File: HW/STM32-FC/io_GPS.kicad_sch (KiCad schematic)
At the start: 4 parts, among them J2 2.54mm Male, Q1 S9013

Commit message: 250102:STM32F407VET
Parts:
- removed J2: 2.54mm Male, Connector_PinHeader_2.54mm:PinHeader_1x03_P2.54mm_Vertical, symbol Connector_Generic:Conn_01x05
- removed Q1: S9013, digikey-footprints:SOT-23-3, symbol Device:Q_NPN_BEC
- removed R5: 1k, Resistor_SMD:R_0402_1005Metric, symbol Device:R_Small_US
- removed R6: 10k, Resistor_SMD:R_0402_1005Metric, symbol Device:R_Small_US
- added J12: Conn_01x06, Connectors_JST:JST_GH_BM06B-GHS-TBT_06x1.25mm_Straight, symbol Connector_Generic:Conn_01x06
- added J13: Conn_01x10, Connectors_JST:JST_GH_BM06B-GHS-TBT_06x1.25mm_Straight, symbol Connector_Generic:Conn_01x10
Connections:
- net +3.3V: now also J13.8 (Pin_8)
- net +5V: now also J12.1 (Pin_1), J13.1 (Pin_1)
- net GND: now also J12.6 (Pin_6), J13.10 (Pin_10)
- new net GPS1_BUZZER: J13.9 (Pin_9)
- new net GPS1_I2C_SCL: J13.4 (Pin_4)
- new net GPS1_I2C_SDA: J13.5 (Pin_5)
- new net GPS1_SW: J13.6 (Pin_6)
- new net GPS1_SW_LED: J13.7 (Pin_7)
- new net GPS1_UART_RX: J13.3 (Pin_3)
- new net GPS1_UART_TX: J13.2 (Pin_2)
- new net GPS2_I2C_SCL: J12.4 (Pin_4)
- new net GPS2_I2C_SDA: J12.5 (Pin_5)
- new net GPS2_UART_RX: J12.3 (Pin_3)
- new net GPS2_UART_TX: J12.2 (Pin_2)
- no-connect marks 1 -> 0

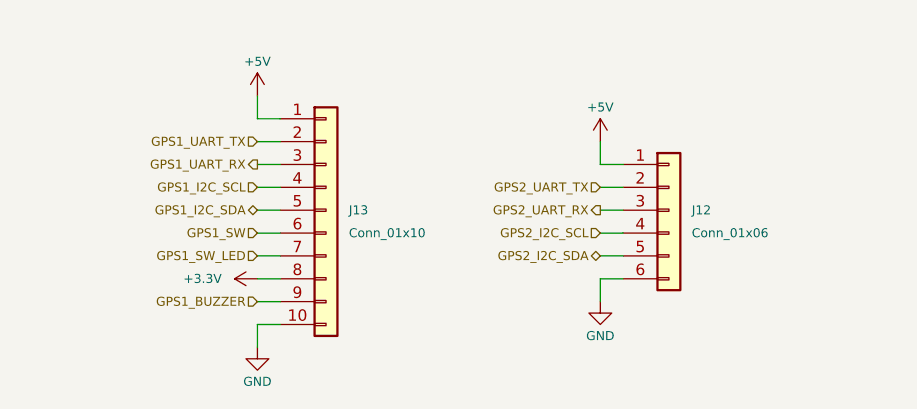
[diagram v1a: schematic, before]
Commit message: RC IN modified
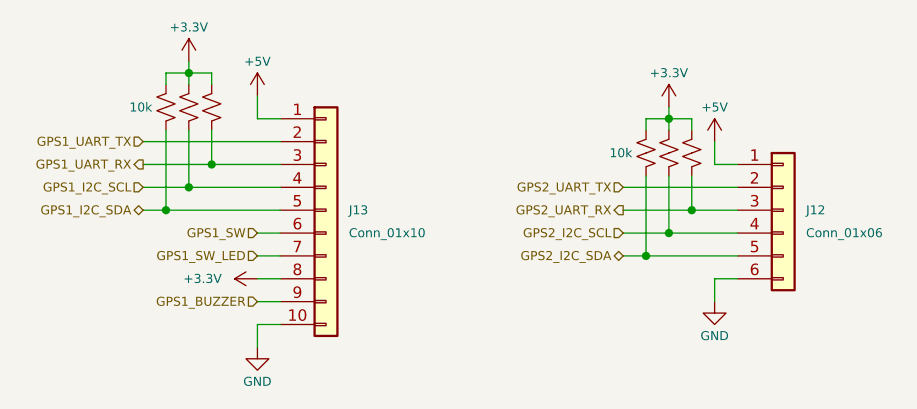
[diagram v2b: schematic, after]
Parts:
- added R18, R19, R20, R21, R22, R4: 10k, Resistor_SMD:R_0402_1005Metric, symbol Device:R_Small_US
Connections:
- net +3.3V: now also R18.1, R19.1, R20.1, R21.1, R22.1, R4.1
- net GPS1_I2C_SCL: now also R18.2
- net GPS1_I2C_SDA: now also R19.2
- net GPS1_UART_RX: now also R4.2
- net GPS2_I2C_SCL: now also R21.2
- net GPS2_I2C_SDA: now also R20.2
- net GPS2_UART_RX: now also R22.2
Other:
- moved on the sheet: J12

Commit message: Big Update:IMU/RC/Conn./MCU
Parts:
- J10: renamed from J12; value Conn_01x06 -> GPS2
- J9: renamed from J13; value Conn_01x10 -> GPS1; footprint Connectors_JST:JST_GH_BM06B-GHS-TBT_06x1.25mm_Straight -> Connectors_JST:JST_GH_BM10B-GHS-TBT_10x1.25mm_Straight
- renumbered R19 to R16, R18 to R17, R20 to R18, R4 to R19, R21 to R20, R22 to R21
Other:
- note added: "GH 1.25mm 10P PC10 : UART4_TX PC11 : UART4_RX PB8 : I2C1_SCL PB9 : I2C1_SDA"
- note added: "GH 1.25mm 6P PC12 : UART5_TX PD2 : UART5_RX PB10 : I2C2_SCL PB11 : I2C2_SDA"
- note added: "GPS1"
- note added: "GPS2"
- company: (none) -> INHA UNIV. NARAE
- title: (none) -> GPS
- moved on the sheet: J10, J9

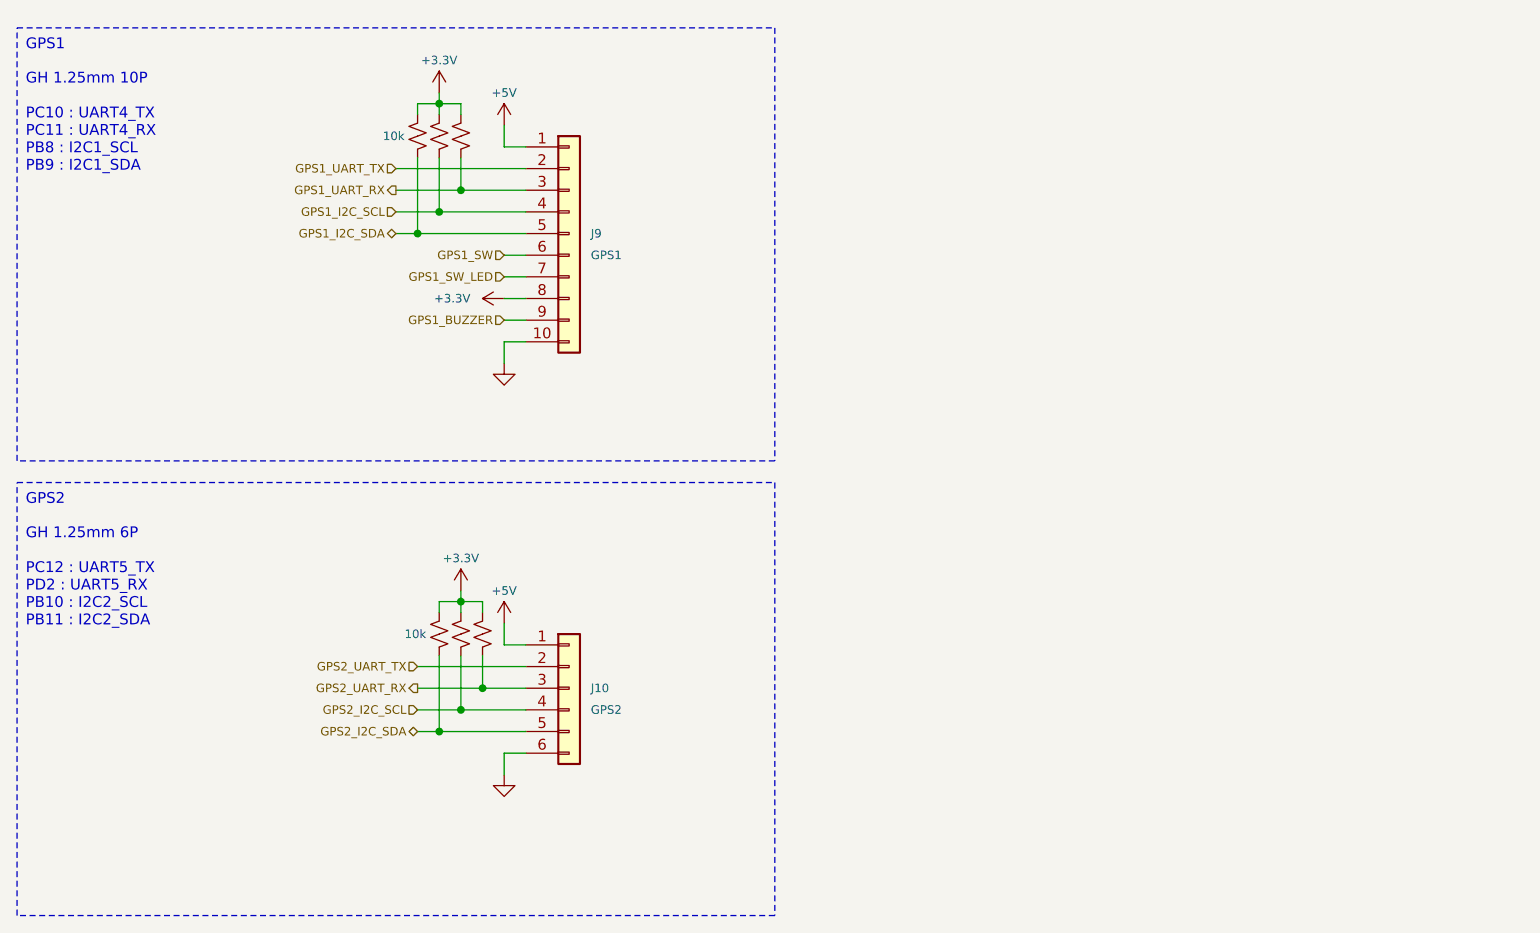
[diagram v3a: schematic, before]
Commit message: 2025.01.03v2:PM(Power Module) added
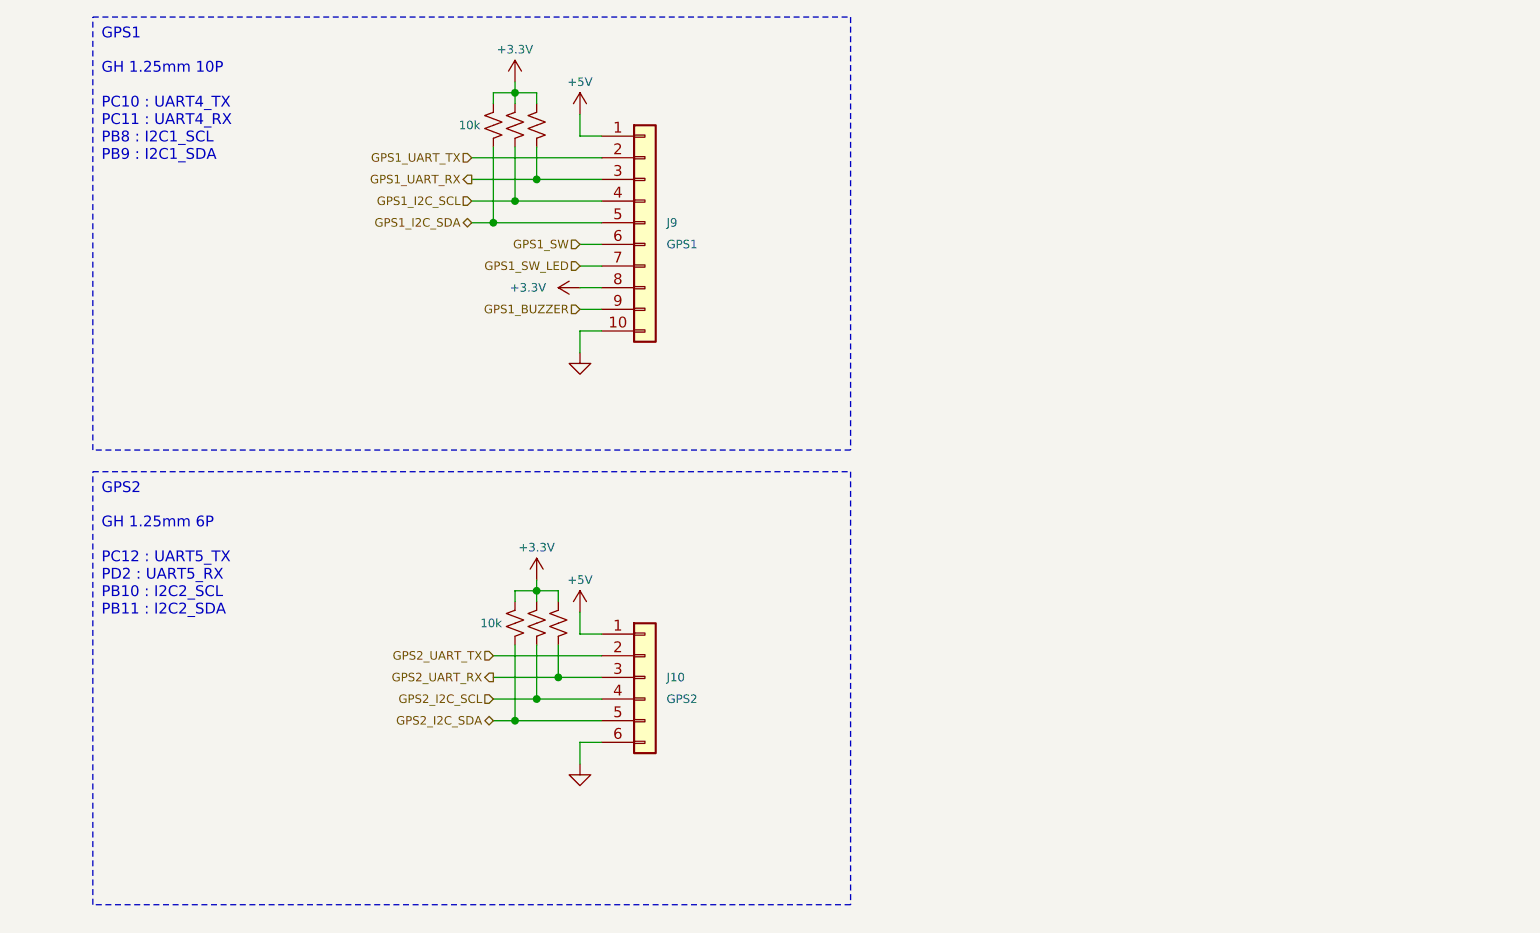
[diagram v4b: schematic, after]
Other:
- company: INHA UNIV. NARAE -> NARAE
- moved on the sheet: J10, J9

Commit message: Baro/SD Card update
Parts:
- J12: renamed from J9; value GPS1 -> GH 1.25mm 10P; footprint Connectors_JST:JST_GH_BM10B-GHS-TBT_10x1.25mm_Straight -> JST_GH:JST_GH_BM10B-GHS-TBT_10
- J13: renamed from J10; value GPS2 -> GH 1.25mm 6P; footprint Connectors_JST:JST_GH_BM06B-GHS-TBT_06x1.25mm_Straight -> JST_GH:JST_GH_BM06B-GHS-TBT_06
- renumbered R16 to R22, R17 to R23, R18 to R24, R19 to R25, R20 to R26, R21 to R27

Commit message: 2025.01.16
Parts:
- renumbered R25 to R24, R24 to R25

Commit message: 2025.01.17 : PCB layout
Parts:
- renumbered J13 to J10, J12 to J9, R22 to R23, R23 to R24, R24 to R26, R26 to R27, R27 to R28
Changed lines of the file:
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@@
 		(shape input)
 		(at 67.31 34.29 180)
-		(fields_autoplaced yes)
 		(effects
 			(font
@@
 		(shape bidirectional)
 		(at 69.85 95.25 180)
-		(fields_autoplaced yes)
 		(effects
 			(font
@@
 		(shape input)
 		(at 80.01 39.37 180)
-		(fields_autoplaced yes)
 		(effects
 			(font
@@
 		(shape input)
 		(at 80.01 41.91 180)
-		(fields_autoplaced yes)
 		(effects
 			(font
@@
 		(shape input)
 		(at 67.31 29.21 180)
-		(fields_autoplaced yes)
 		(effects
 			(font
@@
 		(shape output)
 		(at 67.31 31.75 180)
-		(fields_autoplaced yes)
 		(effects
 			(font
@@
 		(shape bidirectional)
 		(at 67.31 36.83 180)
-		(fields_autoplaced yes)
 		(effects
 			(font
@@
 		(shape input)
 		(at 69.85 92.71 180)
-		(fields_autoplaced yes)
 		(effects
 			(font
@@
 		(shape input)
 		(at 80.01 46.99 180)
-		(fields_autoplaced yes)
 		(effects
 			(font
@@
 		(shape input)
 		(at 69.85 87.63 180)
-		(fields_autoplaced yes)
 		(effects
 			(font
@@
 		(shape output)
 		(at 69.85 90.17 180)
-		(fields_autoplaced yes)
 		(effects
 			(font
@@
 		(on_board yes)
 		(dnp no)
-		(property "Reference" "R27"
+		(property "Reference" "R28"
 			(at 71.12 82.55 0)
 			(effects
@@
 		)
 		(property "SnapEDA_Link" ""
+			(at 77.47 83.82 0)
+			(effects
+				(font
+					(size 1.27 1.27)
+				)
+				(hide yes)
+			)
+		)
+		(property "Sim.Device" ""
+			(at 77.47 83.82 0)
+			(effects
+				(font
+					(size 1.27 1.27)
+				)
+				(hide yes)
+			)
+		)
+		(property "Sim.Pins" ""
 			(at 77.47 83.82 0)
 			(effects
@@
 			(project "STM32-FC"
 				(path "/8d4cc317-3933-4aa6-844b-8c5c635e89c7/20dd612a-0830-4eda-be1e-c1591992c654"
-					(reference "R27")
+					(reference "R28")
 					(unit 1)
 				)
@@
 		(dnp no)
 		(fields_autoplaced yes)
-		(property "Reference" "#PWR092"
+		(property "Reference" "#PWR088"
 			(at 80.01 106.68 0)
 			(effects
@@
 			(project ""
 				(path "/8d4cc317-3933-4aa6-844b-8c5c635e89c7/20dd612a-0830-4eda-be1e-c1591992c654"
-					(reference "#PWR092")
+					(reference "#PWR088")
 					(unit 1)
 				)
@@
 		(dnp no)
 		(fields_autoplaced yes)
-		(property "Reference" "#PWR089"
+		(property "Reference" "#PWR086"
 			(at 80.01 58.42 0)
 			(effects
@@
 			(project ""
 				(path "/8d4cc317-3933-4aa6-844b-8c5c635e89c7/20dd612a-0830-4eda-be1e-c1591992c654"
-					(reference "#PWR089")
+					(reference "#PWR086")
 					(unit 1)
 				)
@@
 		(on_board yes)
 		(dnp no)
-		(property "Reference" "R22"
+		(property "Reference" "R23"
 			(at 62.738 24.13 0)
 			(effects
@@
 		)
 		(property "SnapEDA_Link" ""
+			(at 69.85 25.4 0)
+			(effects
+				(font
+					(size 1.27 1.27)
+				)
+				(hide yes)
+			)
+		)
+		(property "Sim.Device" ""
+			(at 69.85 25.4 0)
+			(effects
+				(font
+					(size 1.27 1.27)
+				)
+				(hide yes)
+			)
+		)
+		(property "Sim.Pins" ""
 			(at 69.85 25.4 0)
 			(effects
@@
 			(project "STM32-FC"
 				(path "/8d4cc317-3933-4aa6-844b-8c5c635e89c7/20dd612a-0830-4eda-be1e-c1591992c654"
-					(reference "R22")
+					(reference "R23")
 					(unit 1)
 				)
@@
 		(dnp no)
 		(fields_autoplaced yes)
-		(property "Reference" "#PWR088"
+		(property "Reference" "#PWR085"
 			(at 83.82 44.45 0)
 			(effects
@@
 			(project ""
 				(path "/8d4cc317-3933-4aa6-844b-8c5c635e89c7/20dd612a-0830-4eda-be1e-c1591992c654"
-					(reference "#PWR088")
+					(reference "#PWR085")
 					(unit 1)
 				)
@@
 		(dnp no)
 		(fields_autoplaced yes)
-		(property "Reference" "#PWR086"
+		(property "Reference" "#PWR082"
 			(at 72.39 24.13 0)
 			(effects
@@
 			(project ""
 				(path "/8d4cc317-3933-4aa6-844b-8c5c635e89c7/20dd612a-0830-4eda-be1e-c1591992c654"
-					(reference "#PWR086")
+					(reference "#PWR082")
 					(unit 1)
 				)
@@
 		(dnp no)
 		(fields_autoplaced yes)
-		(property "Reference" "J12"
+		(property "Reference" "J9"
 			(at 90.17 36.83 0)
 			(effects
@@
 		)
 		(property "SnapEDA_Link" ""
+			(at 87.63 36.83 0)
+			(effects
+				(font
+					(size 1.27 1.27)
+				)
+				(hide yes)
+			)
+		)
+		(property "Sim.Device" ""
+			(at 87.63 36.83 0)
+			(effects
+				(font
+					(size 1.27 1.27)
+				)
+				(hide yes)
+			)
+		)
+		(property "Sim.Pins" ""
 			(at 87.63 36.83 0)
 			(effects
@@
 			(project "STM32-FC"
 				(path "/8d4cc317-3933-4aa6-844b-8c5c635e89c7/20dd612a-0830-4eda-be1e-c1591992c654"
-					(reference "J12")
+					(reference "J9")
 					(unit 1)
 				)
@@
 		(on_board yes)
 		(dnp no)
-		(property "Reference" "R23"
+		(property "Reference" "R24"
 			(at 65.024 24.13 0)
 			(effects
@@
 		)
 		(property "SnapEDA_Link" ""
+			(at 72.39 25.4 0)
+			(effects
+				(font
+					(size 1.27 1.27)
+				)
+				(hide yes)
+			)
+		)
+		(property "Sim.Device" ""
+			(at 72.39 25.4 0)
+			(effects
+				(font
+					(size 1.27 1.27)
+				)
+				(hide yes)
+			)
+		)
+		(property "Sim.Pins" ""
 			(at 72.39 25.4 0)
 			(effects
@@
 			(project "STM32-FC"
 				(path "/8d4cc317-3933-4aa6-844b-8c5c635e89c7/20dd612a-0830-4eda-be1e-c1591992c654"
-					(reference "R23")
+					(reference "R24")
 					(unit 1)
 				)
@@
 		(dnp no)
 		(fields_autoplaced yes)
-		(property "Reference" "J13"
+		(property "Reference" "J10"
 			(at 90.17 90.17 0)
 			(effects
@@
 		)
 		(property "SnapEDA_Link" ""
+			(at 87.63 90.17 0)
+			(effects
+				(font
+					(size 1.27 1.27)
+				)
+				(hide yes)
+			)
+		)
+		(property "Sim.Device" ""
+			(at 87.63 90.17 0)
+			(effects
+				(font
+					(size 1.27 1.27)
+				)
+				(hide yes)
+			)
+		)
+		(property "Sim.Pins" ""
 			(at 87.63 90.17 0)
 			(effects
@@
 			(project "STM32-FC"
 				(path "/8d4cc317-3933-4aa6-844b-8c5c635e89c7/20dd612a-0830-4eda-be1e-c1591992c654"
-					(reference "J13")
+					(reference "J10")
 					(unit 1)
 				)
@@
 		(on_board yes)
 		(dnp no)
-		(property "Reference" "#PWR091"
+		(property "Reference" "#PWR087"
 			(at 80.01 86.36 0)
 			(effects
@@
 			(project ""
 				(path "/8d4cc317-3933-4aa6-844b-8c5c635e89c7/20dd612a-0830-4eda-be1e-c1591992c654"
-					(reference "#PWR091")
+					(reference "#PWR087")
 					(unit 1)
 				)
@@
 		(on_board yes)
 		(dnp no)
-		(property "Reference" "#PWR087"
+		(property "Reference" "#PWR084"
 			(at 80.01 27.94 0)
 			(effects
@@
 			(project ""
 				(path "/8d4cc317-3933-4aa6-844b-8c5c635e89c7/20dd612a-0830-4eda-be1e-c1591992c654"
-					(reference "#PWR087")
+					(reference "#PWR084")
 					(unit 1)
 				)
@@
 		(dnp no)
 		(fields_autoplaced yes)
-		(property "Reference" "#PWR090"
+		(property "Reference" "#PWR083"
 			(at 74.93 82.55 0)
 			(effects
@@
 			(project ""
 				(path "/8d4cc317-3933-4aa6-844b-8c5c635e89c7/20dd612a-0830-4eda-be1e-c1591992c654"
-					(reference "#PWR090")
+					(reference "#PWR083")
 					(unit 1)
 				)
@@
 		(on_board yes)
 		(dnp no)
-		(property "Reference" "R24"
+		(property "Reference" "R26"
 			(at 68.58 24.13 0)
 			(effects
@@
 		)
 		(property "SnapEDA_Link" ""
+			(at 74.93 25.4 0)
+			(effects
+				(font
+					(size 1.27 1.27)
+				)
+				(hide yes)
+			)
+		)
+		(property "Sim.Device" ""
+			(at 74.93 25.4 0)
+			(effects
+				(font
+					(size 1.27 1.27)
+				)
+				(hide yes)
+			)
+		)
+		(property "Sim.Pins" ""
 			(at 74.93 25.4 0)
 			(effects
@@
 			(project "STM32-FC"
 				(path "/8d4cc317-3933-4aa6-844b-8c5c635e89c7/20dd612a-0830-4eda-be1e-c1591992c654"
-					(reference "R24")
+					(reference "R26")
 					(unit 1)
 				)
@@
 		(on_board yes)
 		(dnp no)
-		(property "Reference" "R26"
+		(property "Reference" "R27"
 			(at 67.564 82.55 0)
 			(effects
@@
 		)
 		(property "SnapEDA_Link" ""
+			(at 74.93 83.82 0)
+			(effects
+				(font
+					(size 1.27 1.27)
+				)
+				(hide yes)
+			)
+		)
+		(property "Sim.Device" ""
+			(at 74.93 83.82 0)
+			(effects
+				(font
+					(size 1.27 1.27)
+				)
+				(hide yes)
+			)
+		)
+		(property "Sim.Pins" ""
 			(at 74.93 83.82 0)
 			(effects
@@
 			(project "STM32-FC"
 				(path "/8d4cc317-3933-4aa6-844b-8c5c635e89c7/20dd612a-0830-4eda-be1e-c1591992c654"
-					(reference "R26")
+					(reference "R27")
 					(unit 1)
 				)
@@
 			(at 72.39 83.82 0)
 			(effects
+				(font
+					(size 1.27 1.27)
+				)
+				(hide yes)
+			)
+		)
+		(property "Sim.Device" ""
+			(at 72.39 83.82 0)
+			(effects
+				(font
+					(size 1.27 1.27)
+				)
+				(hide yes)
+			)
+		)
+		(property "Sim.Pins" ""
+			(at 72.39 83.82 0)
+			(effects
